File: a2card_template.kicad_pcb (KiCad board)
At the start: 2 copper layers, 158.8 x 76.4 mm, 10 parts, among them U10 PLCCZ80, U14 74LS367, U15 74LS373, U16 74LS367, U17 74LS367, U9 74LS367

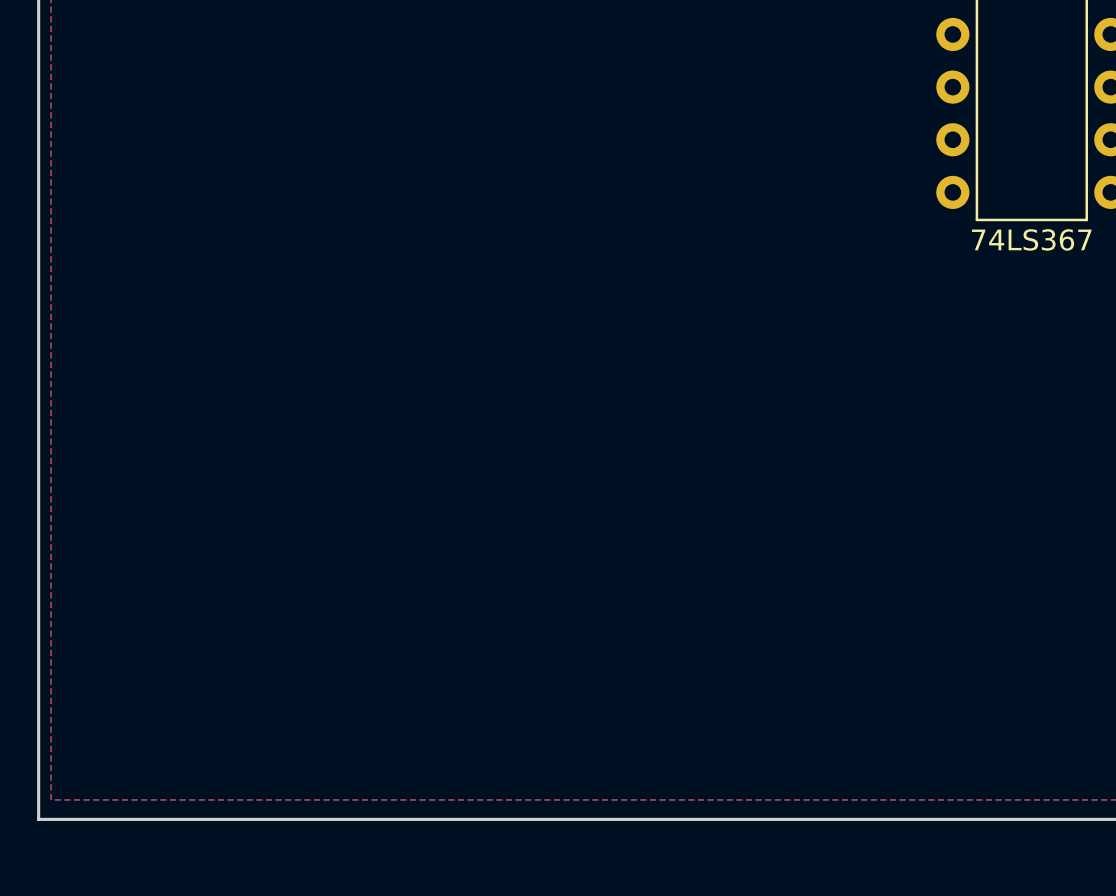
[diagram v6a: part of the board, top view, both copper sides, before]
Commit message: More ICs placed
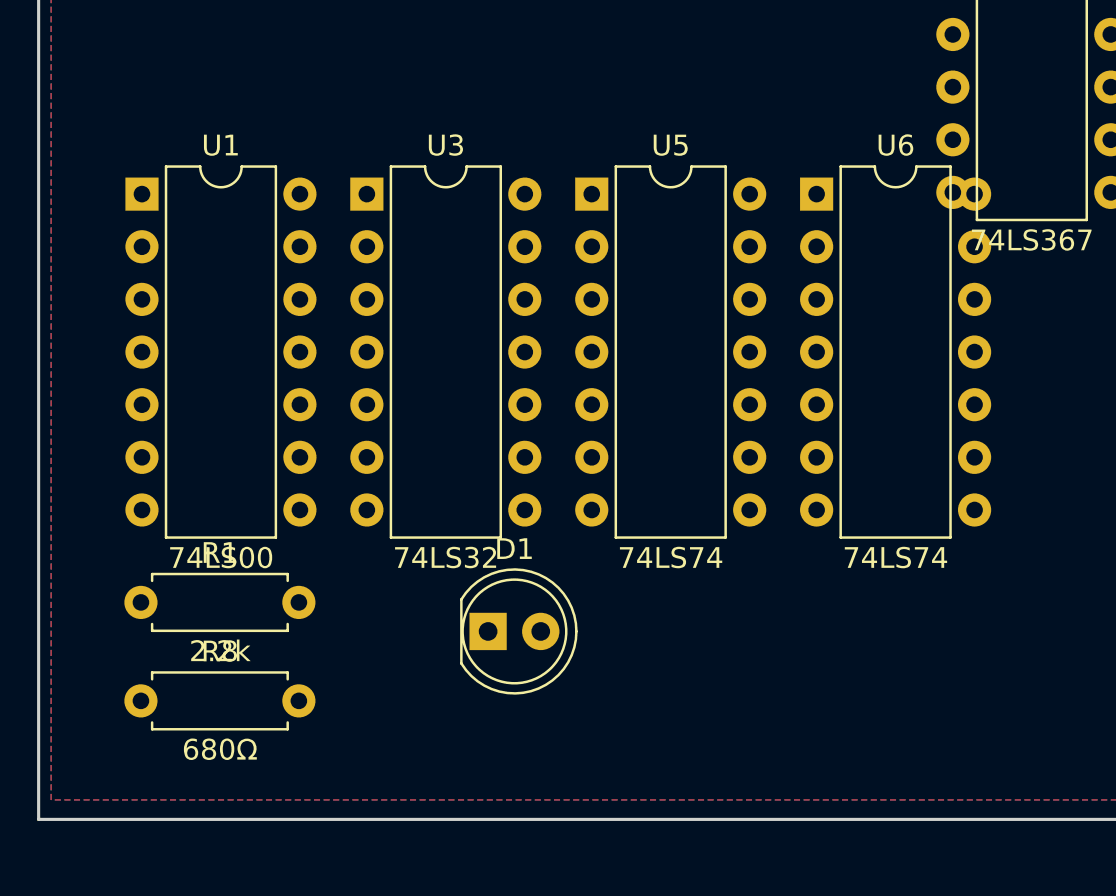
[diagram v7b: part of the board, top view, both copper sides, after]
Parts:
- added D1: LED, LED_THT:LED_D5.0mm, F.Cu at (91.2, 116.3)
- added R1: 2.2k, Resistor_THT:R_Axial_DIN0207_L6.3mm_D2.5mm_P7.62mm_Horizontal, F.Cu at (74.4, 114.9)
- added R8: 680Ω, Resistor_THT:R_Axial_DIN0207_L6.3mm_D2.5mm_P7.62mm_Horizontal, F.Cu at (74.4, 119.7)
- added U1: 74LS00, Package_DIP:DIP-14_W7.62mm, F.Cu at (74.5, 95.2)
- added U3: 74LS32, Package_DIP:DIP-14_W7.62mm, F.Cu at (85.3, 95.2)
- added U5: 74LS74, Package_DIP:DIP-14_W7.62mm, F.Cu at (96.2, 95.2)
- added U6: 74LS74, Package_DIP:DIP-14_W7.62mm, F.Cu at (107.0, 95.2)
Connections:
- BUS1 pad 1: Net-(BUS1-Pad1) -> /~IOSEL
- BUS1 pad 18: Net-(BUS1-Pad18) -> /RW_OUT
- BUS1 pad 31: Net-(BUS1-Pad31) -> /~RESET
- U10 pad 28: Net-(U10-Pad28) -> /~Z80_WAIT
- U10 pad 30: Net-(U10-Pad30) -> /~Z80_RESET
- U16 pad 13: Net-(U16-Pad13) -> /RW_OUT
- U16 pad 14: Net-(U16-Pad14) -> /Z80_RW
- U16 pad 15: Net-(U16-Pad15) -> Net-(U16-Pad1)

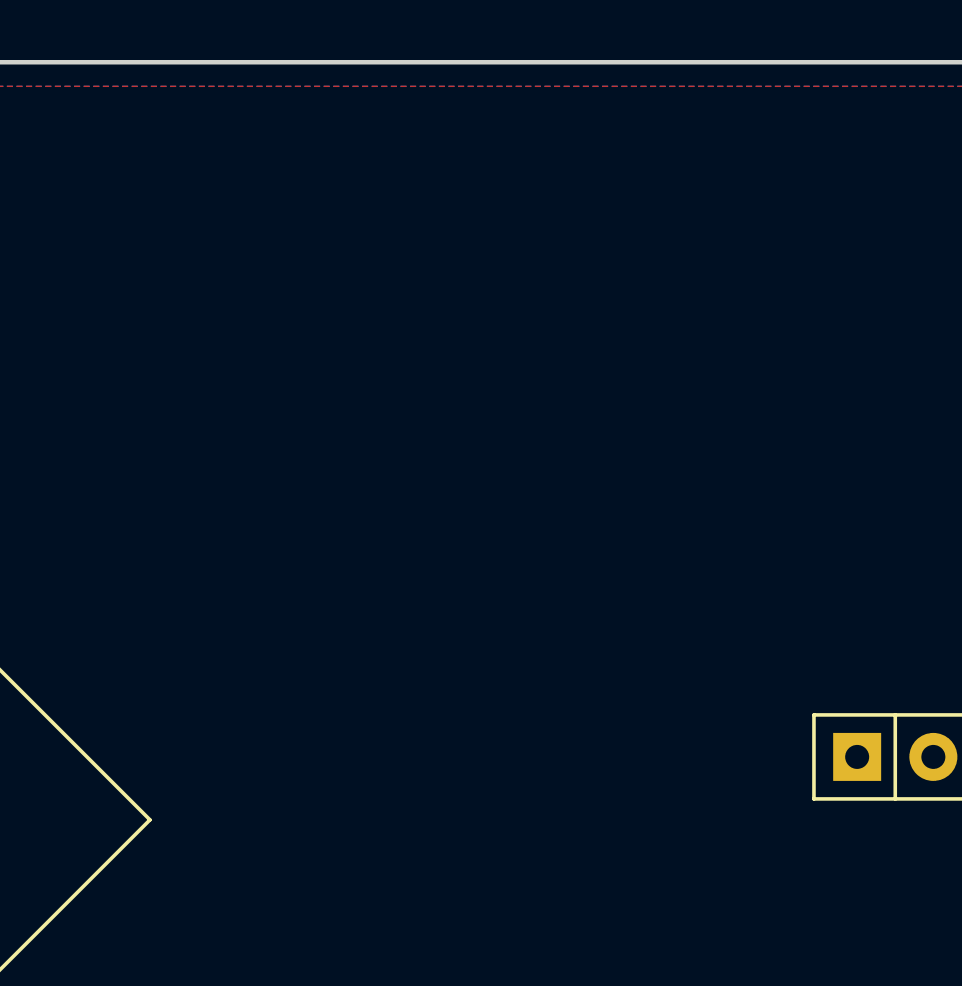
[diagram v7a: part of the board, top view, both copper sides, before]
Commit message: Add u8, part of u7
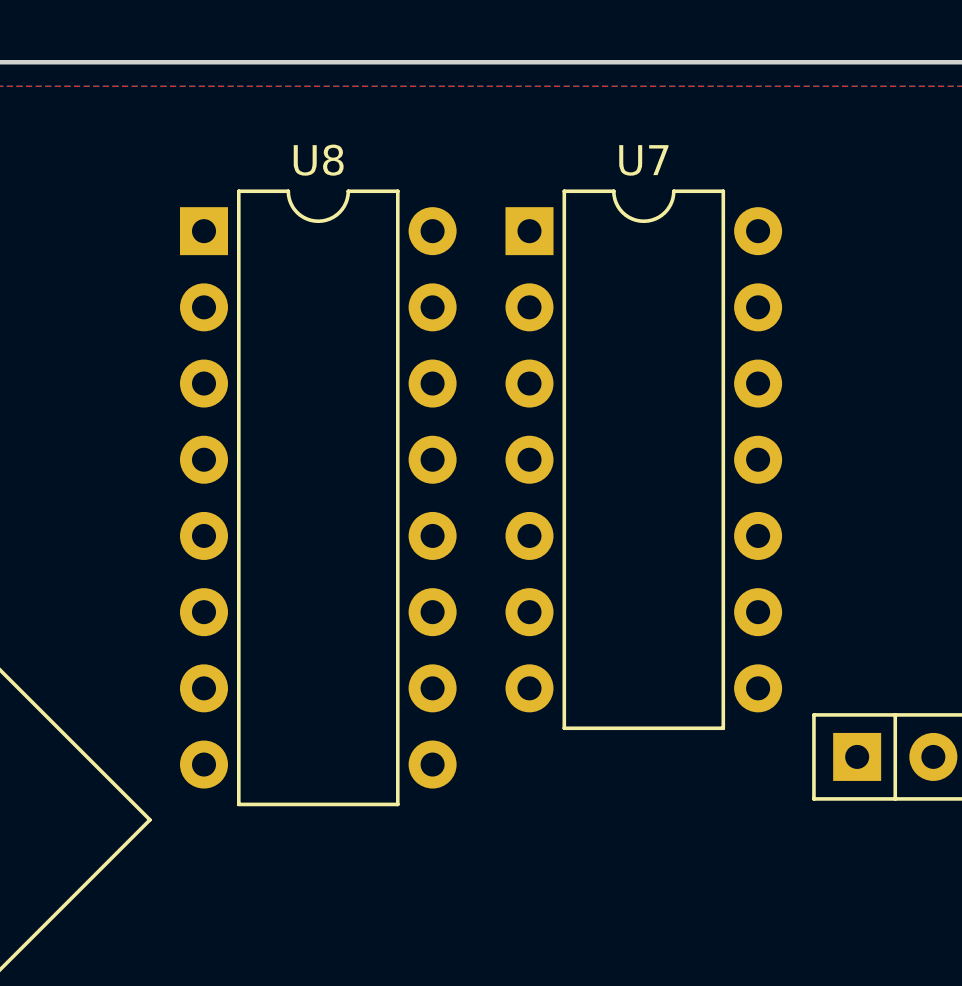
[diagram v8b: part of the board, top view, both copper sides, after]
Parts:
- added U7: 74LS86, Package_DIP:DIP-14_W7.62mm, F.Cu at (174.2, 62.2)
- added U8: 74LS283, Package_DIP:DIP-16_W7.62mm, F.Cu at (163.4, 62.2)
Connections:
- U17 pad 12: /a14' -> Net-(U17-Pad12)
- U17 pad 14: /a13' -> Net-(U17-Pad14)
- U17 pad 2: /a12' -> Net-(U17-Pad2)
- U17 pad 4: /a15' -> Net-(U17-Pad4)
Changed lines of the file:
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@@
     (tracks 8)
     (zones 0)
-    (modules 17)
-    (nets 120)
+    (modules 19)
+    (nets 131)
   )
   (page A4)
@@
   )
   (setup
-    (last_trace_width 1)
+    (last_trace_width 0.25)
     (user_trace_width 0.5)
     (user_trace_width 1)
@@
   (net 118 /Z80_RW)
   (net 119 "Net-(U6-Pad8)")
+  (net 120 "Net-(U7-Pad6)")
+  (net 121 "Net-(U7-Pad4)")
+  (net 122 "Net-(U7-Pad10)")
+  (net 123 "Net-(U7-Pad8)")
+  (net 124 "Net-(U8-Pad7)")
+  (net 125 "Net-(U8-Pad6)")
+  (net 126 "Net-(U17-Pad12)")
+  (net 127 "Net-(U17-Pad2)")
+  (net 128 "Net-(U17-Pad4)")
+  (net 129 "Net-(U8-Pad9)")
+  (net 130 "Net-(U17-Pad14)")
   (net_class Default "To jest domyślna klasa połączeń."
     (clearance 0.2)
@@
     (add_net "Net-(U16-Pad12)")
     (add_net "Net-(U17-Pad1)")
+    (add_net "Net-(U17-Pad12)")
+    (add_net "Net-(U17-Pad14)")
     (add_net "Net-(U17-Pad15)")
+    (add_net "Net-(U17-Pad2)")
+    (add_net "Net-(U17-Pad4)")
     (add_net "Net-(U3-Pad3)")
     (add_net "Net-(U3-Pad5)")
@@
     (add_net "Net-(U6-Pad6)")
     (add_net "Net-(U6-Pad8)")
+    (add_net "Net-(U7-Pad10)")
+    (add_net "Net-(U7-Pad4)")
+    (add_net "Net-(U7-Pad6)")
+    (add_net "Net-(U7-Pad8)")
+    (add_net "Net-(U8-Pad6)")
+    (add_net "Net-(U8-Pad7)")
+    (add_net "Net-(U8-Pad9)")
     (add_net "Net-(U9-Pad1)")
     (add_net "Net-(U9-Pad11)")
@@
     (add_net "Net-(U9-Pad13)")
     (add_net "Net-(U9-Pad14)")
+  )
+  (module Package_DIP:DIP-16_W7.62mm (layer F.Cu)
+    (at 163.394 62.23)
+    (descr "16-lead though-hole mounted DIP package, row spacing 7.62 mm (300 mils)")
+    (tags "THT DIP DIL PDIP 2.54mm 7.62mm 300mil")
+    (fp_text reference U8 (at 3.81 -2.33) (layer F.SilkS)
+      (effects (font (size 1 1) (thickness 0.15)))
+    )
+    (fp_text value 74LS283 (at 3.81 20.11) (layer F.Fab)
+      (effects (font (size 1 1) (thickness 0.15)))
+    )
+    (fp_text user %R (at 3.81 8.89) (layer F.Fab)
+      (effects (font (size 1 1) (thickness 0.15)))
+    )
+    (fp_line (start 8.7 -1.55) (end -1.1 -1.55) (layer F.CrtYd) (width 0.05))
+    (fp_line (start 8.7 19.3) (end 8.7 -1.55) (layer F.CrtYd) (width 0.05))
+    (fp_line (start -1.1 19.3) (end 8.7 19.3) (layer F.CrtYd) (width 0.05))
+    (fp_line (start -1.1 -1.55) (end -1.1 19.3) (layer F.CrtYd) (width 0.05))
+    (fp_line (start 6.46 -1.33) (end 4.81 -1.33) (layer F.SilkS) (width 0.12))
+    (fp_line (start 6.46 19.11) (end 6.46 -1.33) (layer F.SilkS) (width 0.12))
+    (fp_line (start 1.16 19.11) (end 6.46 19.11) (layer F.SilkS) (width 0.12))
+    (fp_line (start 1.16 -1.33) (end 1.16 19.11) (layer F.SilkS) (width 0.12))
+    (fp_line (start 2.81 -1.33) (end 1.16 -1.33) (layer F.SilkS) (width 0.12))
+    (fp_line (start 0.635 -0.27) (end 1.635 -1.27) (layer F.Fab) (width 0.1))
+    (fp_line (start 0.635 19.05) (end 0.635 -0.27) (layer F.Fab) (width 0.1))
+    (fp_line (start 6.985 19.05) (end 0.635 19.05) (layer F.Fab) (width 0.1))
+    (fp_line (start 6.985 -1.27) (end 6.985 19.05) (layer F.Fab) (width 0.1))
+    (fp_line (start 1.635 -1.27) (end 6.985 -1.27) (layer F.Fab) (width 0.1))
+    (fp_arc (start 3.81 -1.33) (end 2.81 -1.33) (angle -180) (layer F.SilkS) (width 0.12))
+    (pad 16 thru_hole oval (at 7.62 0) (size 1.6 1.6) (drill 0.8) (layers *.Cu *.Mask)
+      (net 22 +5V))
+    (pad 8 thru_hole oval (at 0 17.78) (size 1.6 1.6) (drill 0.8) (layers *.Cu *.Mask)
+      (net 21 GND))
+    (pad 15 thru_hole oval (at 7.62 2.54) (size 1.6 1.6) (drill 0.8) (layers *.Cu *.Mask)
+      (net 21 GND))
+    (pad 7 thru_hole oval (at 0 15.24) (size 1.6 1.6) (drill 0.8) (layers *.Cu *.Mask)
+      (net 124 "Net-(U8-Pad7)"))
+    (pad 14 thru_hole oval (at 7.62 5.08) (size 1.6 1.6) (drill 0.8) (layers *.Cu *.Mask)
+      (net 120 "Net-(U7-Pad6)"))
+    (pad 6 thru_hole oval (at 0 12.7) (size 1.6 1.6) (drill 0.8) (layers *.Cu *.Mask)
+      (net 125 "Net-(U8-Pad6)"))
+    (pad 13 thru_hole oval (at 7.62 7.62) (size 1.6 1.6) (drill 0.8) (layers *.Cu *.Mask)
+      (net 126 "Net-(U17-Pad12)"))
+    (pad 5 thru_hole oval (at 0 10.16) (size 1.6 1.6) (drill 0.8) (layers *.Cu *.Mask)
+      (net 123 "Net-(U7-Pad8)"))
+    (pad 12 thru_hole oval (at 7.62 10.16) (size 1.6 1.6) (drill 0.8) (layers *.Cu *.Mask)
+      (net 59 /a15'))
+    (pad 4 thru_hole oval (at 0 7.62) (size 1.6 1.6) (drill 0.8) (layers *.Cu *.Mask)
+      (net 127 "Net-(U17-Pad2)"))
+    (pad 11 thru_hole oval (at 7.62 12.7) (size 1.6 1.6) (drill 0.8) (layers *.Cu *.Mask)
+      (net 21 GND))
+    (pad 3 thru_hole oval (at 0 5.08) (size 1.6 1.6) (drill 0.8) (layers *.Cu *.Mask)
+      (net 60 /a13'))
+    (pad 10 thru_hole oval (at 7.62 15.24) (size 1.6 1.6) (drill 0.8) (layers *.Cu *.Mask)
+      (net 128 "Net-(U17-Pad4)"))
+    (pad 2 thru_hole oval (at 0 2.54) (size 1.6 1.6) (drill 0.8) (layers *.Cu *.Mask)
+      (net 21 GND))
+    (pad 9 thru_hole oval (at 7.62 17.78) (size 1.6 1.6) (drill 0.8) (layers *.Cu *.Mask)
+      (net 129 "Net-(U8-Pad9)"))
+    (pad 1 thru_hole rect (at 0 0) (size 1.6 1.6) (drill 0.8) (layers *.Cu *.Mask)
+      (net 130 "Net-(U17-Pad14)"))
+    (model ${KISYS3DMOD}/Package_DIP.3dshapes/DIP-16_W7.62mm.wrl
+      (at (xyz 0 0 0))
+      (scale (xyz 1 1 1))
+      (rotate (xyz 0 0 0))
+    )
+  )
+  (module Package_DIP:DIP-14_W7.62mm (layer F.Cu)
+    (at 174.244 62.23)
+    (descr "14-lead though-hole mounted DIP package, row spacing 7.62 mm (300 mils)")
+    (tags "THT DIP DIL PDIP 2.54mm 7.62mm 300mil")
+    (fp_text reference U7 (at 3.81 -2.33) (layer F.SilkS)
+      (effects (font (size 1 1) (thickness 0.15)))
+    )
+    (fp_text value 74LS86 (at 3.81 17.57) (layer F.Fab)
+      (effects (font (size 1 1) (thickness 0.15)))
+    )
+    (fp_text user %R (at 3.81 7.62) (layer F.Fab)
+      (effects (font (size 1 1) (thickness 0.15)))
+    )
+    (fp_line (start 8.7 -1.55) (end -1.1 -1.55) (layer F.CrtYd) (width 0.05))
+    (fp_line (start 8.7 16.8) (end 8.7 -1.55) (layer F.CrtYd) (width 0.05))
+    (fp_line (start -1.1 16.8) (end 8.7 16.8) (layer F.CrtYd) (width 0.05))
+    (fp_line (start -1.1 -1.55) (end -1.1 16.8) (layer F.CrtYd) (width 0.05))
+    (fp_line (start 6.46 -1.33) (end 4.81 -1.33) (layer F.SilkS) (width 0.12))
+    (fp_line (start 6.46 16.57) (end 6.46 -1.33) (layer F.SilkS) (width 0.12))
+    (fp_line (start 1.16 16.57) (end 6.46 16.57) (layer F.SilkS) (width 0.12))
+    (fp_line (start 1.16 -1.33) (end 1.16 16.57) (layer F.SilkS) (width 0.12))
+    (fp_line (start 2.81 -1.33) (end 1.16 -1.33) (layer F.SilkS) (width 0.12))
+    (fp_line (start 0.635 -0.27) (end 1.635 -1.27) (layer F.Fab) (width 0.1))
+    (fp_line (start 0.635 16.51) (end 0.635 -0.27) (layer F.Fab) (width 0.1))
+    (fp_line (start 6.985 16.51) (end 0.635 16.51) (layer F.Fab) (width 0.1))
+    (fp_line (start 6.985 -1.27) (end 6.985 16.51) (layer F.Fab) (width 0.1))
+    (fp_line (start 1.635 -1.27) (end 6.985 -1.27) (layer F.Fab) (width 0.1))
+    (fp_arc (start 3.81 -1.33) (end 2.81 -1.33) (angle -180) (layer F.SilkS) (width 0.12))
+    (pad 14 thru_hole oval (at 7.62 0) (size 1.6 1.6) (drill 0.8) (layers *.Cu *.Mask))
+    (pad 7 thru_hole oval (at 0 15.24) (size 1.6 1.6) (drill 0.8) (layers *.Cu *.Mask))
+    (pad 13 thru_hole oval (at 7.62 2.54) (size 1.6 1.6) (drill 0.8) (layers *.Cu *.Mask))
+    (pad 6 thru_hole oval (at 0 12.7) (size 1.6 1.6) (drill 0.8) (layers *.Cu *.Mask)
+      (net 120 "Net-(U7-Pad6)"))
+    (pad 12 thru_hole oval (at 7.62 5.08) (size 1.6 1.6) (drill 0.8) (layers *.Cu *.Mask))
+    (pad 5 thru_hole oval (at 0 10.16) (size 1.6 1.6) (drill 0.8) (layers *.Cu *.Mask)
+      (net 55 /a14'))
+    (pad 11 thru_hole oval (at 7.62 7.62) (size 1.6 1.6) (drill 0.8) (layers *.Cu *.Mask))
+    (pad 4 thru_hole oval (at 0 7.62) (size 1.6 1.6) (drill 0.8) (layers *.Cu *.Mask)
+      (net 121 "Net-(U7-Pad4)"))
+    (pad 10 thru_hole oval (at 7.62 10.16) (size 1.6 1.6) (drill 0.8) (layers *.Cu *.Mask)
+      (net 122 "Net-(U7-Pad10)"))
+    (pad 3 thru_hole oval (at 0 5.08) (size 1.6 1.6) (drill 0.8) (layers *.Cu *.Mask))
+    (pad 9 thru_hole oval (at 7.62 12.7) (size 1.6 1.6) (drill 0.8) (layers *.Cu *.Mask)
+      (net 56 /a12'))
+    (pad 2 thru_hole oval (at 0 2.54) (size 1.6 1.6) (drill 0.8) (layers *.Cu *.Mask))
+    (pad 8 thru_hole oval (at 7.62 15.24) (size 1.6 1.6) (drill 0.8) (layers *.Cu *.Mask)
+      (net 123 "Net-(U7-Pad8)"))
+    (pad 1 thru_hole rect (at 0 0) (size 1.6 1.6) (drill 0.8) (layers *.Cu *.Mask))
+    (model ${KISYS3DMOD}/Package_DIP.3dshapes/DIP-14_W7.62mm.wrl
+      (at (xyz 0 0 0))
+      (scale (xyz 1 1 1))
+      (rotate (xyz 0 0 0))
+    )
   )
   (module Resistor_THT:R_Axial_DIN0207_L6.3mm_D2.5mm_P7.62mm_Horizontal (layer F.Cu)
@@
       (net 28 /a10))
     (pad 14 thru_hole oval (at 7.62 5.08 90) (size 1.6 1.6) (drill 0.8) (layers *.Cu *.Mask)
-      (net 60 /a13'))
+      (net 130 "Net-(U17-Pad14)"))
     (pad 6 thru_hole oval (at 0 12.7 90) (size 1.6 1.6) (drill 0.8) (layers *.Cu *.Mask)
       (net 54 /a10'))
@@
       (net 23 /a15))
     (pad 12 thru_hole oval (at 7.62 10.16 90) (size 1.6 1.6) (drill 0.8) (layers *.Cu *.Mask)
-      (net 55 /a14'))
+      (net 126 "Net-(U17-Pad12)"))
     (pad 4 thru_hole oval (at 0 7.62 90) (size 1.6 1.6) (drill 0.8) (layers *.Cu *.Mask)
-      (net 59 /a15'))
+      (net 128 "Net-(U17-Pad4)"))
     (pad 11 thru_hole oval (at 7.62 12.7 90) (size 1.6 1.6) (drill 0.8) (layers *.Cu *.Mask)
       (net 24 /a14))
@@
       (net 61 /a11'))
     (pad 2 thru_hole oval (at 0 2.54 90) (size 1.6 1.6) (drill 0.8) (layers *.Cu *.Mask)
-      (net 56 /a12'))
+      (net 127 "Net-(U17-Pad2)"))
     (pad 9 thru_hole oval (at 7.62 17.78 90) (size 1.6 1.6) (drill 0.8) (layers *.Cu *.Mask)
       (net 27 /a11))
